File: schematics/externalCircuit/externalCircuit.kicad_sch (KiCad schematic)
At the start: 4 parts

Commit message: add details to schematic
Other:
- company: (none) -> UIndy Physics/RB Annis School of Engineering
- title: (none) -> Tiny PCB Circuit
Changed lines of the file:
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@@
 	(generator_version "8.0")
 	(paper "A4")
+	(title_block
+		(title "Tiny PCB Circuit")
+		(date "2024-12-30")
+		(company "UIndy Physics/RB Annis School of Engineering")
+		(comment 1 "External Circuit for Intro Projects")
+	)
 	(junction
 		(at 45.72 27.94)

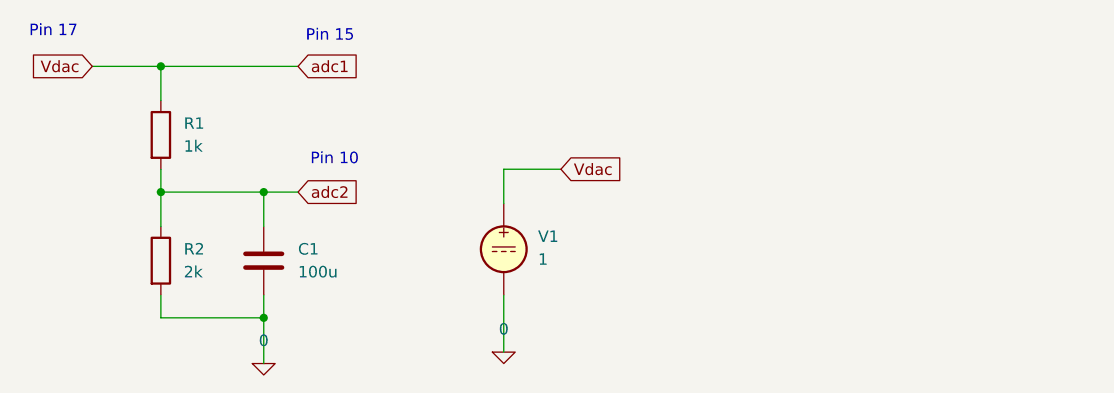
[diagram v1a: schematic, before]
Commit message: update schematic
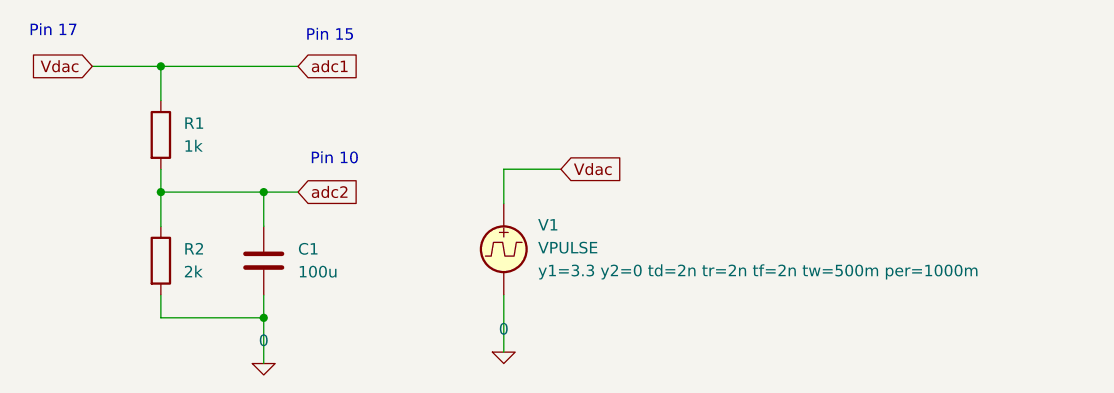
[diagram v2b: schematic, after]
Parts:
- removed V1: 1, symbol Simulation_SPICE:VDC
- added V1: VPULSE, symbol Simulation_SPICE:VPULSE
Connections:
- net 0: now also V1.2
- net Vdac: now also V1.1
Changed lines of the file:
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@@
 	)
 	(symbol
-		(lib_id "Simulation_SPICE:VDC")
+		(lib_id "Simulation_SPICE:VPULSE")
 		(at 83.82 48.26 0)
 		(unit 1)
@@
 		(fields_autoplaced yes)
 		(property "Reference" "V1"
-			(at 87.63 46.8601 0)
+			(at 87.63 45.5901 0)
 			(effects
 				(font
@@
 			)
 		)
-		(property "Value" "1"
-			(at 87.63 49.4001 0)
+		(property "Value" "VPULSE"
+			(at 87.63 48.1301 0)
 			(effects
 				(font
@@
 			)
 		)
-		(property "Description" "Voltage source, DC"
+		(property "Description" "Voltage source, pulse"
 			(at 83.82 48.26 0)
 			(effects
@@
 			)
 		)
-		(property "Sim.Type" "DC"
+		(property "Sim.Type" "PULSE"
 			(at 83.82 48.26 0)
 			(effects
@@
 			)
 		)
+		(property "Sim.Params" "y1=3.3 y2=0 td=2n tr=2n tf=2n tw=500m per=1000m"
+			(at 87.63 50.6701 0)
+			(effects
+				(font
+					(size 1.27 1.27)
+				)
+				(justify left)
+			)
+		)
